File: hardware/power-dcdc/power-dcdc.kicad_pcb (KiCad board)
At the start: 2 copper layers, 110 x 70 mm, 69 parts, among them J1 SOLAR_IN, J2 DCDC-MEASURES, J3 DCDC-PWM, J4 BATT2, J5 BATT1, Q1 SIR164ADP, Q2 SIR164ADP, Q3 SI7149ADP, Q4 SI7149ADP, Q5 SI7149ADP, Q6 SI7149ADP, U1 LP4951C, U2 NCP5901B, U3 PAC1953-1, U4 DGD0215, U5 DGD0215

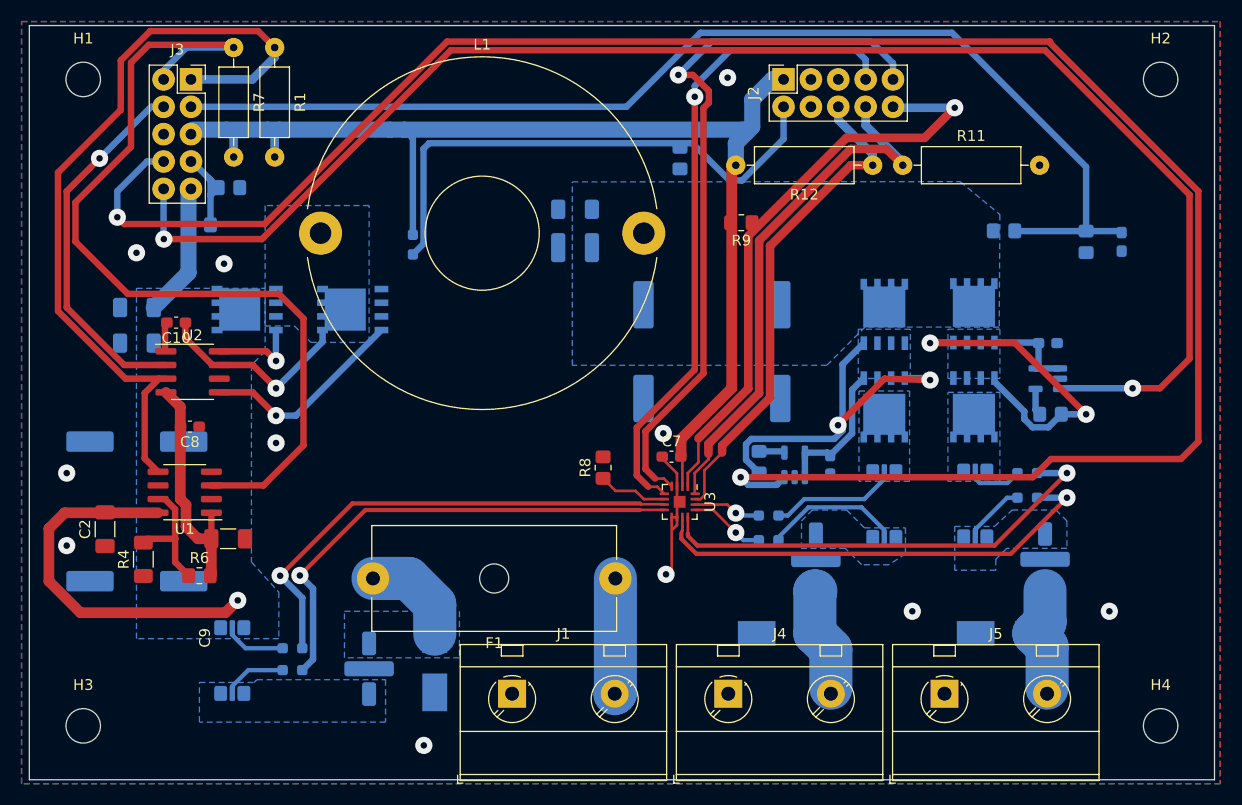
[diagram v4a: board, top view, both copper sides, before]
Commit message: Connect mounting holes to GND
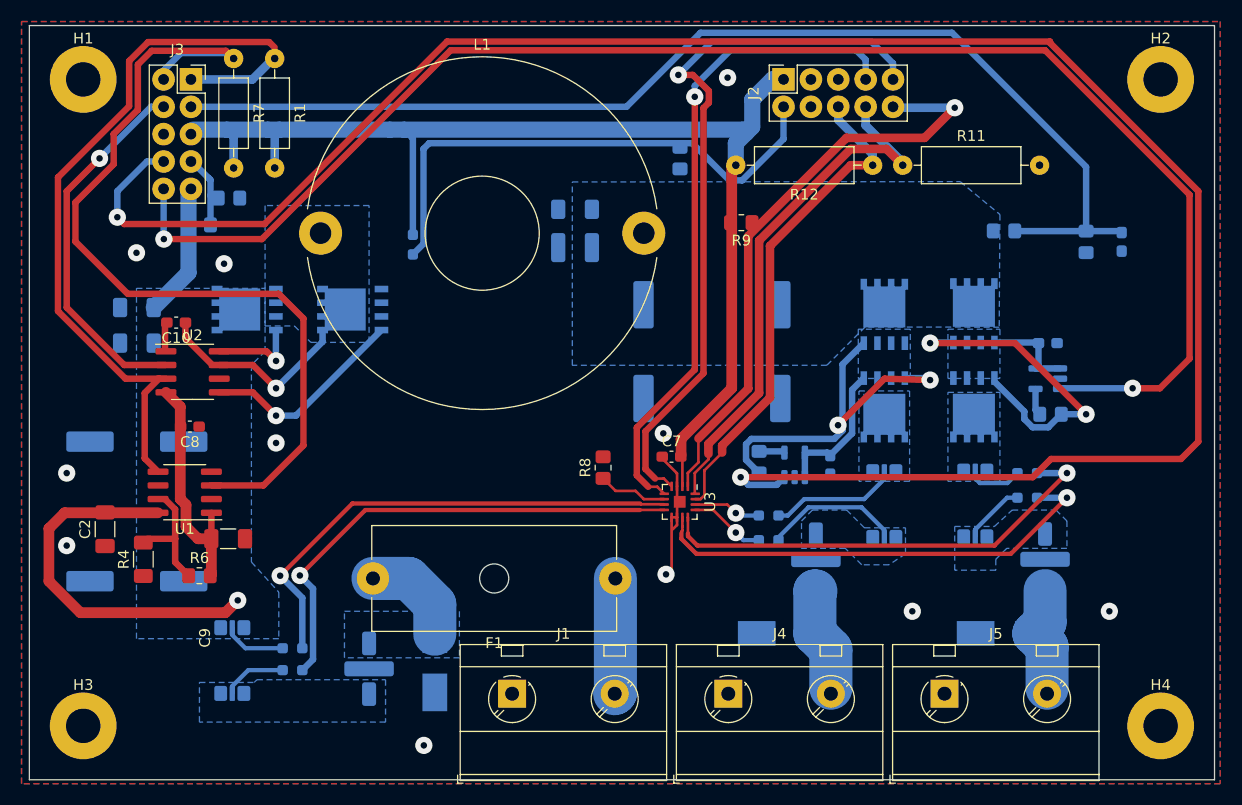
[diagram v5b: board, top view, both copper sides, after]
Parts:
- H1, H2, H3, H4: value MountingHole -> MountingHole_Pad; footprint MountingHole:MountingHole_3.2mm_M3_DIN965 -> MountingHole:MountingHole_3.2mm_M3_DIN965_Pad
- moved R1 1.02 mm to (72.8, 83.1)
- moved R7 1.02 mm to (69.0, 83.1)
- moved R3 0.97 mm to (68.5, 96.0)
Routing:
- net /PWM_OK: track 73.6 -> 71.2 mm
- net /Solar_V: track 8.87 -> 6.59 mm
- net +5V: track 109.2 -> 111.3 mm

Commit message: Change some resistor values to match available ones.
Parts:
- R17: value 157k -> 158k
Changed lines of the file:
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@@
       (effects (font (size 1 1) (thickness 0.15)) (justify mirror))
     )
-    (fp_text value "157k" (at 0 -1.65) (layer "B.Fab")
+    (fp_text value "158k" (at 0 -1.65) (layer "B.Fab")
       (effects (font (size 1 1) (thickness 0.15)) (justify mirror))
     )

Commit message: one more track cleanup
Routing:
- net Net-(C16-Pad1): track 10.00 -> 14.7 mm
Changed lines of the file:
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@@
   (segment (start 121.981 119.6395) (end 124.058 119.6395) (width 0.6) (layer "B.Cu") (net 11))
   (segment (start 126.365 113.8055) (end 126.365 117.856) (width 0.6) (layer "B.Cu") (net 11))
-  (segment (start 144.46 141.506) (end 144.46 137.658) (width 4) (layer "B.Cu") (net 12))
-  (segment (start 143.228 136.426) (end 144.272 135.382) (width 4) (layer "B.Cu") (net 12))
-  (segment (start 144.272 135.382) (end 144.272 132.45) (width 4) (layer "B.Cu") (net 12))
-  (segment (start 144.46 137.658) (end 143.228 136.426) (width 4) (layer "B.Cu") (net 12))
+  (segment (start 144.272 137.47) (end 143.228 136.426) (width 4) (layer "B.Cu") (net 12))
+  (segment (start 144.272 141.826) (end 144.272 132.45) (width 4) (layer "B.Cu") (net 12))
+  (segment (start 144.272 141.318) (end 144.272 137.47) (width 4) (layer "B.Cu") (net 12))
   (segment (start 143.6635 109.474) (end 143.6635 111.551) (width 0.6) (layer "B.Cu") (net 13))
   (segment (start 143.3885 111.826) (end 145.6635 111.826) (width 0.6) (layer "B.Cu") (net 13))

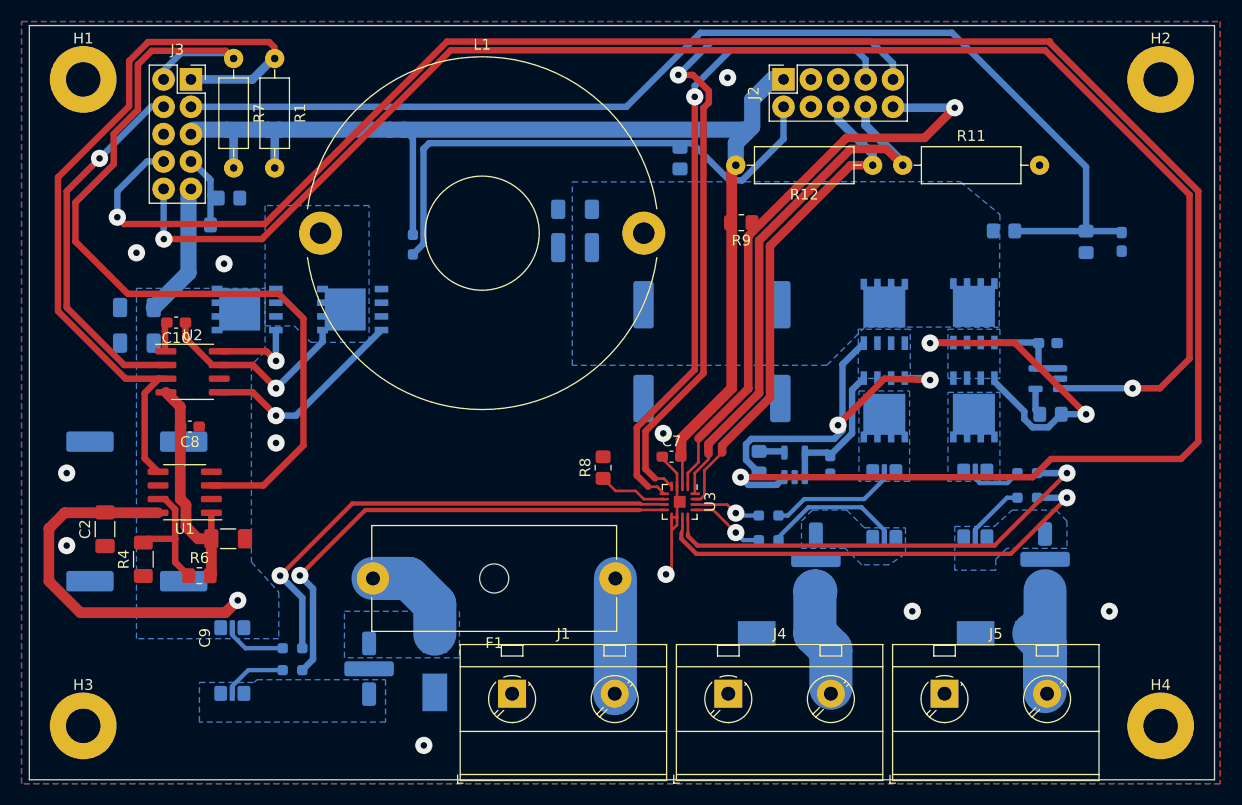
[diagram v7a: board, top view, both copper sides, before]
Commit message: power-dcdc: increase clearance where possible; cleanup tracks
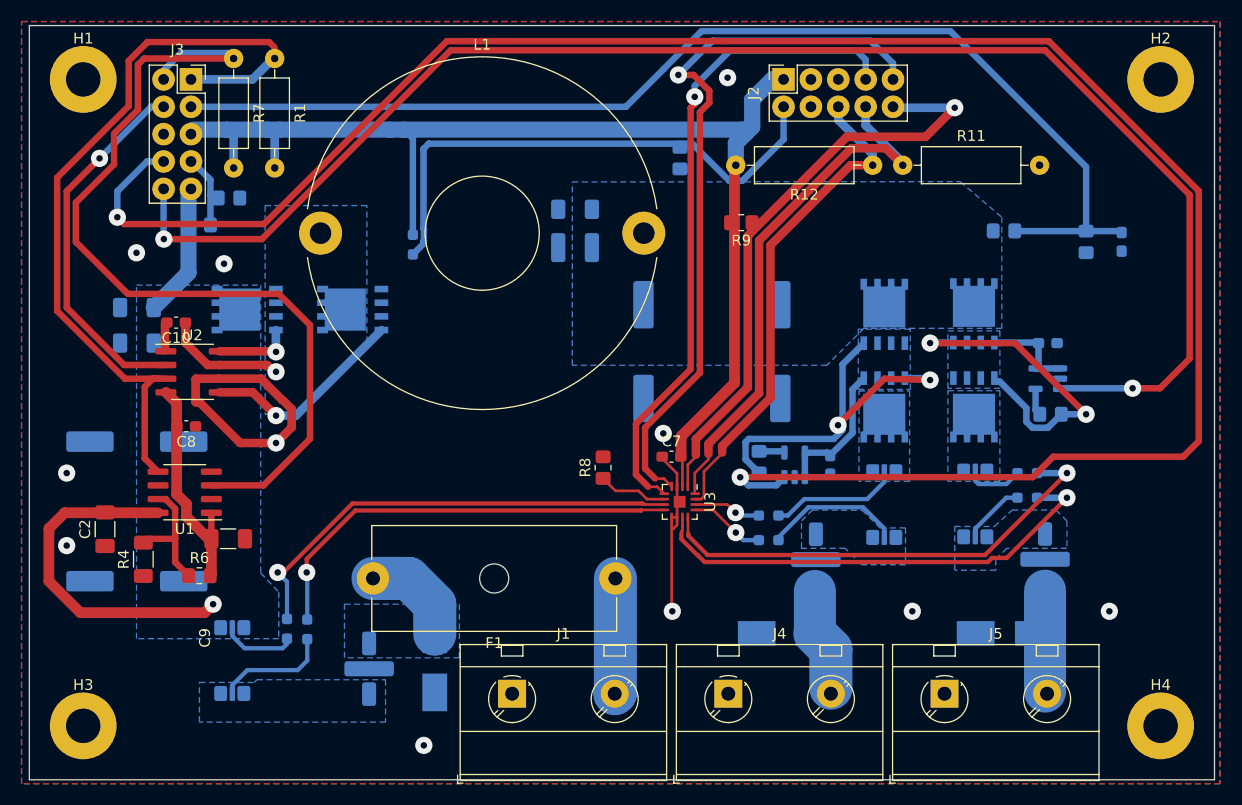
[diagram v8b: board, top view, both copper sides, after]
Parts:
- moved F3 4.03 mm to (75.8, 136.0), turned to -90 degrees
- moved F2 1.87 mm to (73.9, 136.0), turned to -90 degrees
- moved C8 0.33 mm to (64.6, 117.2)
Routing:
- net GND: track 13.0 -> 41.3 mm
- net Net-(C10-Pad1): track 18.3 -> 11.4 mm
- net Net-(F3-Pad1): track 46.0 -> 40.7 mm
- net Net-(C16-Pad1): track 14.7 -> 9.38 mm
- net Net-(F3-Pad2): track 5.97 -> 10.7 mm
- net Net-(F2-Pad1): track 46.0 -> 43.2 mm
- net /SOLAR_PWR: track 47.3 -> 44.8 mm
- net Net-(Q1-Pad4): track 8.51 -> 7.32 mm
- net Net-(F2-Pad2): track 5.86 -> 6.97 mm
- net Net-(F6-Pad2): track 42.8 -> 43.5 mm
- net /+7V: track 21.9 -> 21.4 mm
- net Net-(F7-Pad2): track 43.4 -> 44.0 mm
